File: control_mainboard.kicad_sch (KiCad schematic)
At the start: 59 parts, among them J1 USB_C_Receptacle_USB2.0_14P, J18 SM03B-SRSS-TB, J2 [battery], J3 SD_Card_Receptacle, J4 [bootstrap jumper], J8 FFC Connector, Q1 DMG3415, Q2 DMG3415, SW1 [reset button], SW5 SW_SPST, U1 RP2350A, U2 XC6220B331MR, U3 MCP73831-2-OT, U4 W25Q128JVS, Y1 ABM8-272-T3

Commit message: simplified card detect/write protect
read the datasheet wrong, can just use the write protect pin, it's open when inserted card is write protected and also when there is no card, and pulled down when a card that is write enabled is inserted, so it can also work as a card detect.
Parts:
- removed Q?: Si1308EDL, Package_TO_SOT_SMD:SOT-323_SC-70, symbol Transistor_FET:Si1308EDL
- removed R30, R31: 10k, Resistor_SMD:R_1206_3216Metric, symbol Device:R_Small
- added R29: 10k, Resistor_SMD:R_1206_3216Metric, symbol Device:R_Small
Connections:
- net CARD_DETECT is gone; now on net SD_WP: U1.3 (GPIO1)
- net +3V3: now also R29.1
- net SD_WP: now also R29.2
- net SD_CD: no longer names the net of J3.10 (CARD_DETECT)
- no-connect marks 2 -> 3
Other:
- note removed: "lock card detect high (card not detected) if write protect is enabled"

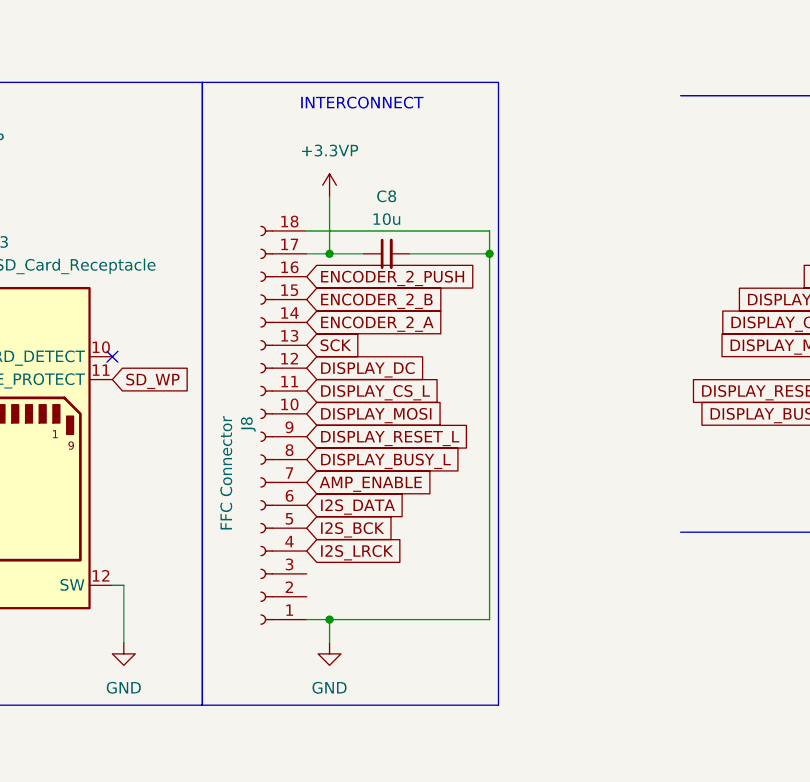
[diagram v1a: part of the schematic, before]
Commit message: update left/right interconnect
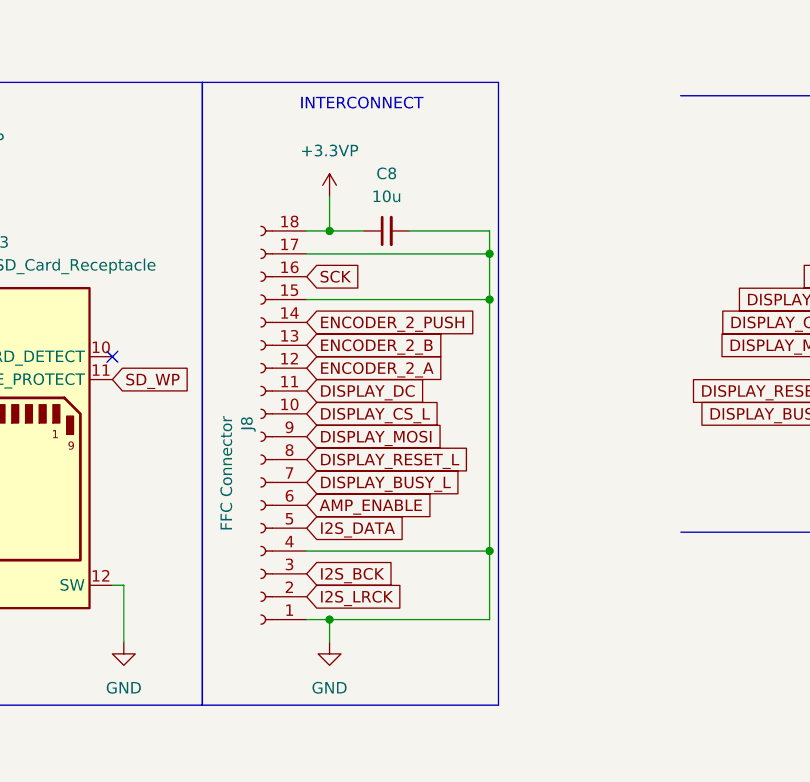
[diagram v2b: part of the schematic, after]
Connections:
- net +3.3VP: now also J8.18 (Pin_18); no longer J8.17 (Pin_17)
- net AMP_ENABLE: now also J8.6 (Pin_6); no longer J8.7 (Pin_7)
- net DISPLAY_BUSY_L: now also J8.7 (Pin_7); no longer J8.8 (Pin_8)
- net DISPLAY_CS_L: now also J8.10 (Pin_10); no longer J8.11 (Pin_11)
- net DISPLAY_DC: now also J8.11 (Pin_11); no longer J8.12 (Pin_12)
- net DISPLAY_MOSI: now also J8.9 (Pin_9); no longer J8.10 (Pin_10)
- net DISPLAY_RESET_L: now also J8.8 (Pin_8); no longer J8.9 (Pin_9)
- net ENCODER_2_A: now also J8.12 (Pin_12); no longer J8.14 (Pin_14)
- net ENCODER_2_B: now also J8.13 (Pin_13); no longer J8.15 (Pin_15)
- net ENCODER_2_PUSH: now also J8.14 (Pin_14); no longer J8.16 (Pin_16)
- net GND: now also J8.15 (Pin_15), J8.17 (Pin_17), J8.4 (Pin_4); no longer J8.18 (Pin_18)
- net I2S_BCK: now also J8.3 (Pin_3); no longer J8.5 (Pin_5)
- net I2S_DATA: now also J8.5 (Pin_5); no longer J8.6 (Pin_6)
- net I2S_LRCK: now also J8.2 (Pin_2); no longer J8.4 (Pin_4)
- net SCK: now also J8.16 (Pin_16); no longer J8.13 (Pin_13)
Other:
- moved on the sheet: C8
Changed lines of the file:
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@@
 	)
 	(junction
-		(at 167.64 328.93)
-		(diameter 0)
-		(color 0 0 0 0)
-	)
-	(junction
 		(at -29.21 233.68)
 		(diameter 0)
@@
 	)
 	(junction
-		(at 185.42 328.93)
-		(diameter 0)
-		(color 0 0 0 0)
-	)
-	(junction
 		(at -31.75 379.73)
 		(diameter 0)
@@
 	)
 	(junction
+		(at 167.64 326.39)
+		(diameter 0)
+		(color 0 0 0 0)
+	)
+	(junction
+		(at 185.42 361.95)
+		(diameter 0)
+		(color 0 0 0 0)
+	)
+	(junction
 		(at 252.73 109.22)
 		(diameter 0)
@@
 	)
 	(junction
+		(at 185.42 328.93)
+		(diameter 0)
+		(color 0 0 0 0)
+	)
+	(junction
 		(at 219.71 92.71)
 		(diameter 0)
@@
 	)
 	(junction
+		(at 185.42 334.01)
+		(diameter 0)
+		(color 0 0 0 0)
+	)
+	(junction
 		(at 229.87 100.33)
 		(diameter 0)
@@
 	(wire
 		(pts
+			(xy 165.1 361.95) (xy 185.42 361.95)
+		)
+		(stroke
+			(width 0)
+			(type default)
+		)
+	)
+	(wire
+		(pts
 			(xy 66.04 347.98) (xy 50.8 347.98)
 		)
@@
 	(wire
 		(pts
-			(xy 167.64 328.93) (xy 171.45 328.93)
+			(xy 167.64 326.39) (xy 171.45 326.39)
 		)
 		(stroke
@@
 	(wire
 		(pts
+			(xy 165.1 334.01) (xy 185.42 334.01)
+		)
+		(stroke
+			(width 0)
+			(type default)
+		)
+	)
+	(wire
+		(pts
 			(xy -49.53 359.41) (xy -48.26 359.41)
 		)
@@
 	(wire
 		(pts
-			(xy 165.1 326.39) (xy 185.42 326.39)
-		)
-		(stroke
-			(width 0)
-			(type default)
-		)
-	)
-	(wire
-		(pts
 			(xy 1.27 379.73) (xy 1.27 359.41)
 		)
@@
 	(wire
 		(pts
+			(xy 165.1 328.93) (xy 185.42 328.93)
+		)
+		(stroke
+			(width 0)
+			(type default)
+		)
+	)
+	(wire
+		(pts
 			(xy 167.64 369.57) (xy 185.42 369.57)
 		)
@@
 	(wire
 		(pts
-			(xy 165.1 328.93) (xy 167.64 328.93)
+			(xy 288.29 120.65) (xy 284.48 120.65)
 		)
 		(stroke
@@
 	(wire
 		(pts
-			(xy 288.29 120.65) (xy 284.48 120.65)
+			(xy 185.42 328.93) (xy 185.42 334.01)
 		)
 		(stroke
@@
 	(wire
 		(pts
+			(xy 185.42 334.01) (xy 185.42 361.95)
+		)
+		(stroke
+			(width 0)
+			(type default)
+		)
+	)
+	(wire
+		(pts
 			(xy 265.43 102.87) (xy 265.43 104.14)
 		)
@@
 	(wire
 		(pts
-			(xy 167.64 322.58) (xy 167.64 328.93)
+			(xy 167.64 322.58) (xy 167.64 326.39)
 		)
 		(stroke
@@
 	(wire
 		(pts
+			(xy 165.1 326.39) (xy 167.64 326.39)
+		)
+		(stroke
+			(width 0)
+			(type default)
+		)
+	)
+	(wire
+		(pts
 			(xy 228.6 140.97) (xy 229.87 140.97)
 		)
@@
 	(wire
 		(pts
-			(xy 185.42 328.93) (xy 185.42 369.57)
-		)
-		(stroke
-			(width 0)
-			(type default)
-		)
-	)
-	(wire
-		(pts
 			(xy 199.39 99.06) (xy 199.39 100.33)
 		)
@@
 	(wire
 		(pts
+			(xy 185.42 361.95) (xy 185.42 369.57)
+		)
+		(stroke
+			(width 0)
+			(type default)
+		)
+	)
+	(wire
+		(pts
 			(xy 111.76 361.95) (xy 111.76 364.49)
 		)
@@
 	(wire
 		(pts
-			(xy 176.53 328.93) (xy 185.42 328.93)
+			(xy 176.53 326.39) (xy 185.42 326.39)
 		)
 		(stroke
@@
 	(global_label "I2S_LRCK"
 		(shape input)
-		(at 165.1 361.95 0)
+		(at 165.1 367.03 0)
 		(fields_autoplaced yes)
 		(effects
@@
 		)
 		(property "Intersheetrefs" "${INTERSHEET_REFS}"
-			(at 176.9147 361.95 0)
+			(at 176.9147 367.03 0)
 			(effects
 				(font
@@
 	(global_label "ENCODER_2_B"
 		(shape input)
-		(at 165.1 334.01 0)
+		(at 165.1 339.09 0)
 		(fields_autoplaced yes)
 		(effects
@@
 		)
 		(property "Intersheetrefs" "${INTERSHEET_REFS}"
-			(at 181.2689 334.01 0)
+			(at 181.2689 339.09 0)
 			(effects
 				(font
@@
 	(global_label "DISPLAY_CS_L"
 		(shape input)
-		(at 165.1 344.17 0)
+		(at 165.1 346.71 0)
 		(fields_autoplaced yes)
 		(effects
@@
 		)
 		(property "Intersheetrefs" "${INTERSHEET_REFS}"
-			(at 181.0876 344.17 0)
+			(at 181.0876 346.71 0)
 			(effects
 				(font
@@
 	(global_label "I2S_DATA"
 		(shape input)
-		(at 165.1 356.87 0)
+		(at 165.1 359.41 0)
 		(fields_autoplaced yes)
 		(effects
@@
 		)
 		(property "Intersheetrefs" "${INTERSHEET_REFS}"
-			(at 176.4914 356.87 0)
+			(at 176.4914 359.41 0)
 			(effects
 				(font
@@
 	(global_label "DISPLAY_DC"
 		(shape input)
-		(at 165.1 341.63 0)
+		(at 165.1 344.17 0)
 		(fields_autoplaced yes)
 		(effects
@@
 		)
 		(property "Intersheetrefs" "${INTERSHEET_REFS}"
-			(at 179.1524 341.63 0)
+			(at 179.1524 344.17 0)
 			(effects
 				(font
@@
 	(global_label "ENCODER_2_A"
 		(shape input)
-		(at 165.1 336.55 0)
+		(at 165.1 341.63 0)
 		(fields_autoplaced yes)
 		(effects
@@
 		)
 		(property "Intersheetrefs" "${INTERSHEET_REFS}"
-			(at 181.0875 336.55 0)
+			(at 181.0875 341.63 0)
 			(effects
 				(font
@@
 	(global_label "DISPLAY_RESET_L"
 		(shape input)
-		(at 165.1 349.25 0)
+		(at 165.1 351.79 0)
 		(fields_autoplaced yes)
 		(effects
@@
 		)
 		(property "Intersheetrefs" "${INTERSHEET_REFS}"
-			(at 184.3532 349.25 0)
+			(at 184.3532 351.79 0)
 			(effects
 				(font
@@
 	(global_label "DISPLAY_BUSY_L"
 		(shape input)
-		(at 165.1 351.79 0)
+		(at 165.1 354.33 0)
 		(fields_autoplaced yes)
 		(effects
@@
 		)
 		(property "Intersheetrefs" "${INTERSHEET_REFS}"
-			(at 183.5067 351.79 0)
+			(at 183.5067 354.33 0)
 			(effects
 				(font
@@
 	(global_label "ENCODER_2_PUSH"
 		(shape input)
-		(at 165.1 331.47 0)
+		(at 165.1 336.55 0)
 		(fields_autoplaced yes)
 		(effects
@@
 		)
 		(property "Intersheetrefs" "${INTERSHEET_REFS}"
-			(at 185.1394 331.47 0)
+			(at 185.1394 336.55 0)
 			(effects
 				(font
@@
 	(global_label "SCK"
 		(shape input)
-		(at 165.1 339.09 0)
+		(at 165.1 331.47 0)
 		(fields_autoplaced yes)
 		(effects
@@
 		)
 		(property "Intersheetrefs" "${INTERSHEET_REFS}"
-			(at 171.8347 339.09 0)
+			(at 171.8347 331.47 0)
 			(effects
 				(font
@@
 	(global_label "I2S_BCK"
 		(shape input)
-		(at 165.1 359.41 0)
+		(at 165.1 364.49 0)
 		(fields_autoplaced yes)
 		(effects
@@
 		)
 		(property "Intersheetrefs" "${INTERSHEET_REFS}"
-			(at 175.8866 359.41 0)
+			(at 175.8866 364.49 0)
 			(effects
 				(font
@@
 	(global_label "AMP_ENABLE"
 		(shape input)
-		(at 165.1 354.33 0)
+		(at 165.1 356.87 0)
 		(fields_autoplaced yes)
 		(effects
@@
 		)
 		(property "Intersheetrefs" "${INTERSHEET_REFS}"
-			(at 179.878 354.33 0)
+			(at 179.878 356.87 0)
 			(effects
 				(font
@@
 	(global_label "DISPLAY_MOSI"
 		(shape input)
-		(at 165.1 346.71 0)
+		(at 165.1 349.25 0)
 		(fields_autoplaced yes)
 		(effects
@@
 		)
 		(property "Intersheetrefs" "${INTERSHEET_REFS}"
-			(at 181.2086 346.71 0)
+			(at 181.2086 349.25 0)
 			(effects
 				(font
@@
 	(symbol
 		(lib_id "Device:C_Small")
-		(at 173.99 328.93 90)
+		(at 173.99 326.39 90)
 		(unit 1)
 		(exclude_from_sim no)
@@
 		(fields_autoplaced yes)
 		(property "Reference" "C8"
-			(at 173.9963 322.58 90)
+			(at 173.9963 320.04 90)
 			(effects
 				(font
@@
 		)
 		(property "Value" "10u"
-			(at 173.9963 325.12 90)
+			(at 173.9963 322.58 90)
 			(effects
 				(font
@@
 		)
 		(property "Footprint" "Capacitor_SMD:C_0805_2012Metric"
-			(at 173.99 328.93 0)
+			(at 173.99 326.39 0)
 			(effects
 				(font
@@
 		)
 		(property "Datasheet" "~"
-			(at 173.99 328.93 0)
+			(at 173.99 326.39 0)
 			(effects
 				(font
@@
 		)
 		(property "Description" "Unpolarized capacitor, small symbol"
-			(at 173.99 328.93 0)
+			(at 173.99 326.39 0)
 			(effects
 				(font

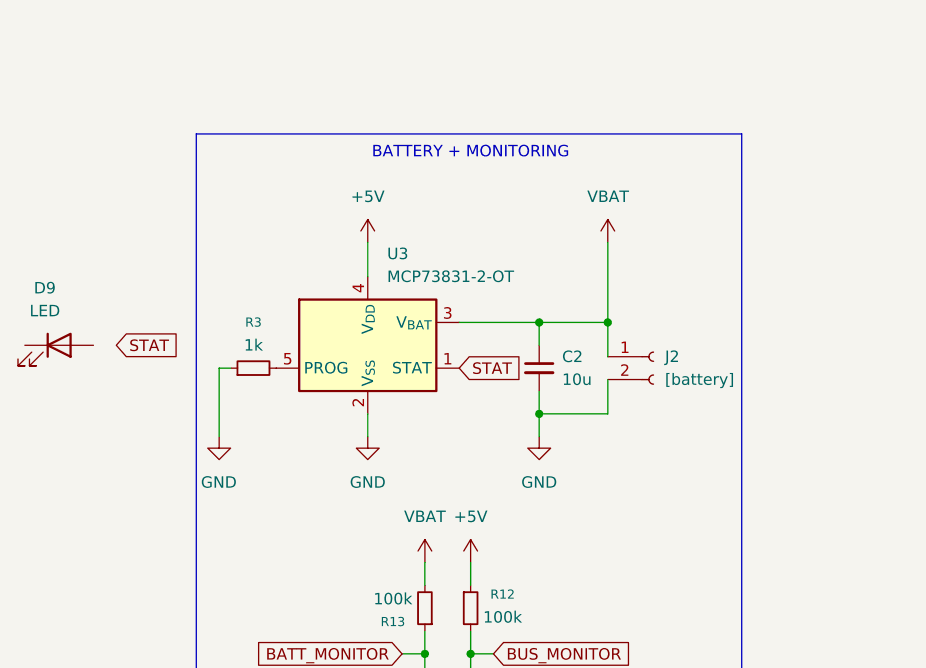
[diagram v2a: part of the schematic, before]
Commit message: charge status LED
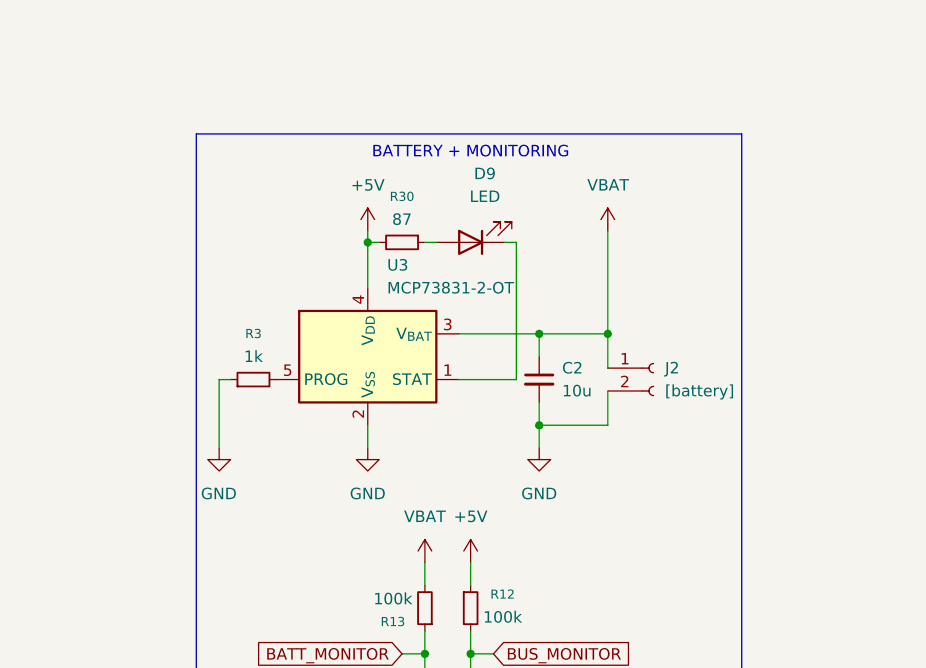
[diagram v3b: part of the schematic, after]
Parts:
- added R30: 87, Resistor_SMD:R_1206_3216Metric, symbol Device:R_Small
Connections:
- net STAT is gone; now on an unnamed net: U3.1 (STAT)
- net +5V: now also R30.2
- net at D9.2 (A): now also R30.1
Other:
- moved on the sheet: C2, D9, J2, R3, U3

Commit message: updating schematic
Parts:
- removed R7: 10k, Resistor_SMD:R_1206_3216Metric, symbol Device:R_Small
- added C221: 100n, Capacitor_SMD:C_1206_3216Metric, symbol Device:C_Small
- added U205: 74AHC1G04, Package_TO_SOT_SMD:SOT-23, symbol 74xGxx:74AHC1G04
- D201: renamed from D9; footprint (none) -> LED_SMD:LED_0603_1608Metric
- gave numbers to parts that had none: 2
- renumbered C2 to C201, C1 to C202, C3 to C203, C68 to C204, C8 to C205, C14 to C206, C15 to C207, C13 to C208, C12 to C209, C17 to C210, C16 to C211, C11 to C212, C10 to C213, C9 to C215, C7 to C216, C67 to C217, C4 to C218, C6 to C219, C5 to C220, D4 to D202, J1 to J201, J2 to J202, J3 to J203, J8 to J204, J4 to J205, J18 to J206, L3 to L201, Q1 to Q201, Q2 to Q202, R3 to R201, R30 to R202, R13 to R203, R14 to R204, R1 to R205, R2 to R206, R12 to R207, R15 to R208, R4 to R209, R9 to R211, R8 to R212, R40 to R213, R10 to R215, R5 to R216, R6 to R217, R16 to R218, R29 to R219, R11 to R220, SW1 to SW201, SW5 to SW202, U3 to U201, U2 to U202, U4 to U203, U1 to U204, Y1 to Y201
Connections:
- net MISO is gone; now on net SD_D0: J203.7 (DAT0)
- net MOSI is gone; now on net SD_CMD: J203.2 (CMD)
- net SD_CS is gone; now on net SD_D3: J203.1 (CD/DAT3)
- net +3V3: now also C221.1, U205.5 (VCC)
- net DISPLAY_CS_L: now also U205.4; no longer U204.13 (GPIO9)
- net DISPLAY_CS_R: now also U205.2
- net GND: now also C221.2, U205.3 (GND)
- net SCK: no longer J203.5 (CLK)
- net SD_CLK: now also J203.5 (CLK)
- net SD_D1: now also J203.8 (DAT1)
- net SD_D2: now also J203.9 (DAT2)
- net at R220.2, SW202.1 (A): now also U204.13 (GPIO9); no longer U204.2 (GPIO0)
- new net FLASH_SEL: U204.2 (GPIO0)
- no-connect marks 3 -> 1
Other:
- note removed: "sleep switch"
- moved on the sheet: C201, C202, C203, C204, C205, C206, C207, C208, C209, C210, C211, C212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

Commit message: added secondary flash to schematic
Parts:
- removed J205: [bootstrap jumper], Connector_PinHeader_1.00mm:PinHeader_1x02_P1.00mm_Vertical, symbol Connector:Conn_01x02_Pin
- removed R213: 0, Resistor_SMD:R_0402_1005Metric, symbol Device:R
- added C207: 100n, Capacitor_SMD:C_1206_3216Metric, symbol Device:C_Small
- added R219: 10k, Resistor_SMD:R_1206_3216Metric, symbol Device:R_Small
- added SW202: [reset button], Button_Switch_SMD:Panasonic_EVQPUK_EVQPUB, symbol Switch:SW_Push
- added U203: W25Q128JVS, Package_SO:SOIC-8_5.3x5.3mm_P1.27mm, symbol Memory_Flash:W25Q128JVS
- SW201: value [reset button] -> [bootstrap button]
- renumbered C203 to C201, C201 to C202, C202 to C203, C206 to C205, C205 to C206, C212 to C210, C210 to C211, C211 to C212, C207 to C221, C221 to C222, J203 to J202, J202 to J203, J206 to J205, R211 to R210, R212 to R211, R214 to R212, R215 to R213, R216 to R214, R217 to R215, R218 to R216, R219 to R217, R220 to R218, SW202 to SW203, U203 to U206
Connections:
- net +3V3: now also C207.2, R219.1, U203.8 (VCC)
- net GND: now also SW201.2, C207.1, U203.4 (GND)
- net QSPI_SCLK: now also U203.6 (CLK)
- net at R210.1: now also SW201.1
- net QSPI_D1: now reaches U204.59 (QSPI_SD1), U206.2 (DO/IO_{1})
- net QSPI_D1: now also U203.2 (DO/IO_{1})
- net QSPI_D2: now reaches U204.58 (QSPI_SD2), U206.3 (~{WP}/IO_{2})
- net QSPI_D2: now also U203.3 (~{WP}/IO_{2})
- net QSPI_D0: now reaches U204.57 (QSPI_SD0), U206.5 (DI/IO_{0})
- net QSPI_D0: now also U203.5 (DI/IO_{0})
- net QSPI_D3: now reaches U204.55 (QSPI_SD3), U206.7 (~{HOLD}/~{RESET}/IO_{3})
- net QSPI_D3: now also U203.7 (~{HOLD}/~{RESET}/IO_{3})
- net at R212.2: now also SW202.1; no longer SW201.1
- net at U204.26 (RUN): now also SW202.2; no longer SW201.2
- net FLASH_CS_1: now reaches U204.60 (~{QSPI_SS})
- net FLASH_CS_1: now also R210.2, R211.1, U203.1 (~{CS})
- removed net FLASH_CS: R210.2, R211.1, U206.1 (~{CS})
- net FLASH_SEL renamed FLASH_CS_2
- net FLASH_CS_2: now also U206.1 (~{CS}), R219.2
- net VREG_AVDD: no longer names the net of C214.1, R216.1, U204.46 (VREG_AVDD)
- net VREG_LX: no longer names the net of L201.2, U204.48 (VREG_LX)
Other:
- note added: "PRIMARY FLASH"
- note added: "SECONDARY FLASH"
- note removed: "placing jumper between pins of J4 and reseting will put RP2040 into BOOTSEL mode instead of running contents of flash storage"
- moved on the sheet: C204, C205, C208, C209, C210, C211, C212, C213, C214, C215, C216, C217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
